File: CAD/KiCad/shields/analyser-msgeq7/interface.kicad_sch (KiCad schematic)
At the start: 3 parts

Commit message: Route the shield set and validate shared interfaces
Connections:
- net +5V: no longer names the net of JA1.23
- no-connect marks 0 -> 1
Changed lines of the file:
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@@
 (kicad_sch (version 20250114) (generator "eeschema") (generator_version "9.0")
  (paper "A3")
-          (title_block (title "analyser-msgeq7 / interface") (date "2026-10-01") (rev "A-review")
+          (title_block (title "analyser-msgeq7 / interface") (date "2026-10-04") (rev "A-prototype")
             (company "Colloquy of Mobiles") (comment 1 "Prototype: verify harness polarity and sensor values before connection"))
           (text "COLLOQUY / ANALYSER-MSGEQ7 / INTERFACE" (at 15.24 15.24 0) (effects (font (size 2.032 2.032) (bold yes)) (justify left top)))
@@
 (wire (pts (xy 121.9200 104.1400) (xy 124.4600 104.1400)) (stroke (width 0) (type default)))
 (global_label "GND" (shape bidirectional) (at 124.4600 104.1400 0) (effects (font (size 0.95 0.95)) (justify left)) (property "Intersheetrefs" "${INTERSHEET_REFS}" (at 124.4600 104.1400 0) (effects (font (size 1.016 1.016))  (hide yes))))
-(wire (pts (xy 121.9200 109.2200) (xy 124.4600 109.2200)) (stroke (width 0) (type default)))
-(global_label "+5V" (shape bidirectional) (at 124.4600 109.2200 0) (effects (font (size 0.95 0.95)) (justify left)) (property "Intersheetrefs" "${INTERSHEET_REFS}" (at 124.4600 109.2200 0) (effects (font (size 1.016 1.016))  (hide yes))))
+(no_connect (at 121.9200 109.2200))
 (symbol (lib_id "Colloquy:H1") (at 66.0400 154.9400 0) (unit 1) (exclude_from_sim no) (in_bom no) (on_board yes) (dnp no)
 (property "Reference" "H1" (at 66.0400 139.7000 0) (effects (font (size 1.016 1.016))  ))

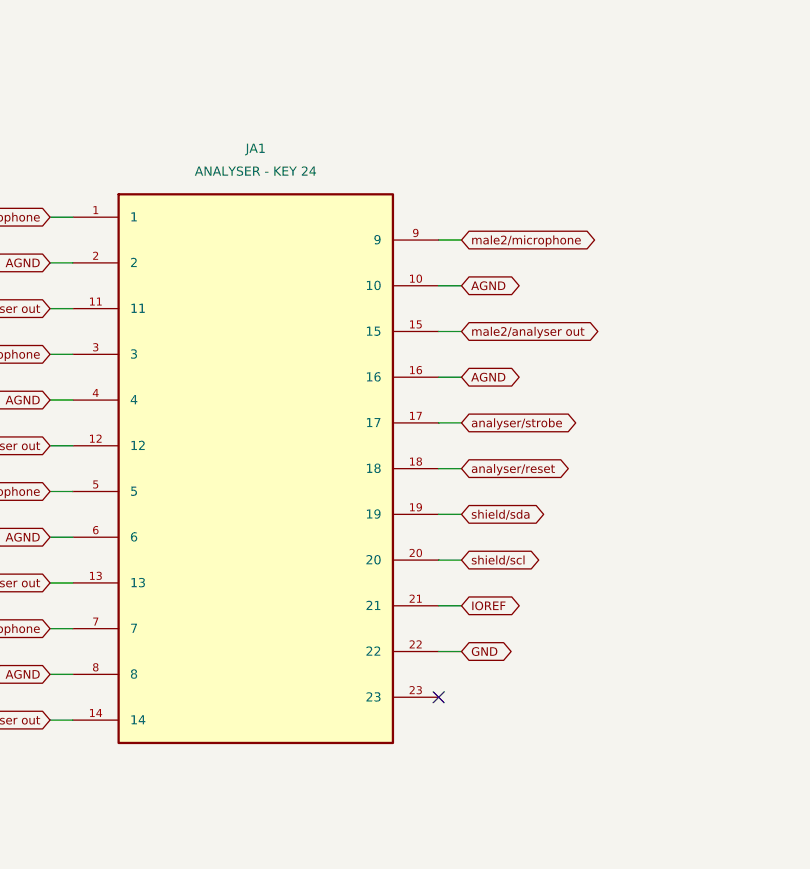
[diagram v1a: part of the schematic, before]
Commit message: Remove shield identification and adopt the simplified connector and Teensy pin maps
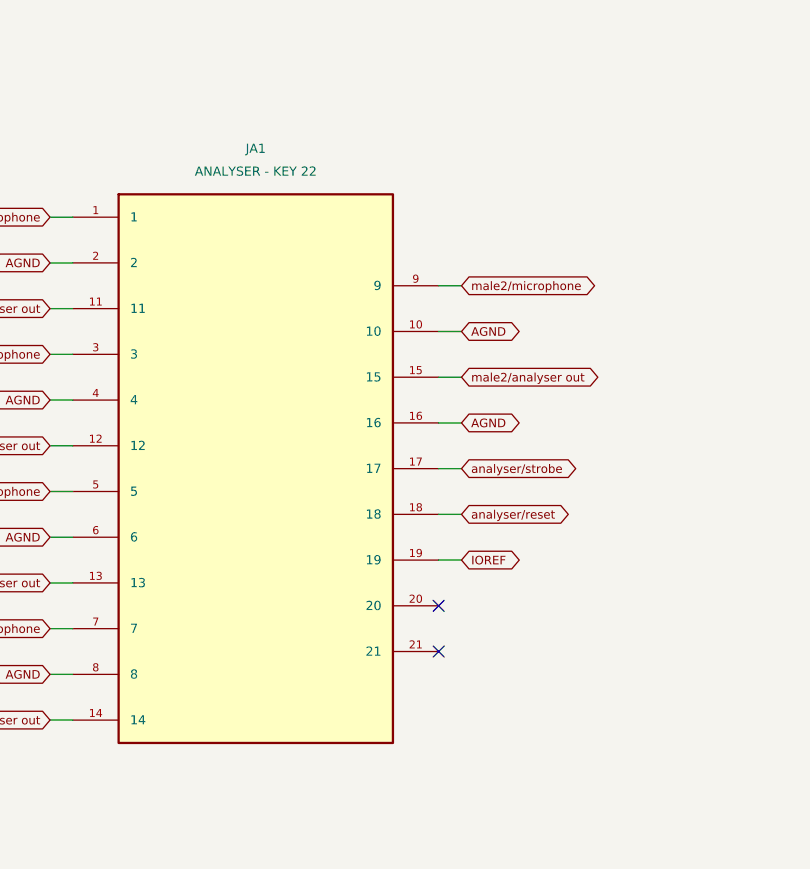
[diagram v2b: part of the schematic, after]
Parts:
- JA1: value ANALYSER - KEY 24 -> ANALYSER - KEY 22; footprint Shields:Socket_2x12_Key24 -> Shields:Socket_2x11_Key22
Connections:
- net shield/sda is gone; now on net IOREF: JA1.19
- net IOREF: no longer JA1.21
- removed net GND: JA1.22
- net shield/scl: no longer names the net of JA1.20
- no-connect marks 1 -> 2
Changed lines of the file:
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@@
 (symbol (lib_id "Colloquy:JA1") (at 101.6000 83.8200 0) (unit 1) (exclude_from_sim no) (in_bom yes) (on_board yes) (dnp no)
 (property "Reference" "JA1" (at 101.6000 48.2600 0) (effects (font (size 1.016 1.016))  ))
-(property "Value" "ANALYSER - KEY 24" (at 101.6000 50.8000 0) (effects (font (size 1.016 1.016))  ))
-(property "Footprint" "Shields:Socket_2x12_Key24" (at 101.6000 83.8200 0) (effects (font (size 1.27 1.27))  (hide yes)))
+(property "Value" "ANALYSER - KEY 22" (at 101.6000 50.8000 0) (effects (font (size 1.016 1.016))  ))
+(property "Footprint" "Shields:Socket_2x11_Key22" (at 101.6000 83.8200 0) (effects (font (size 1.27 1.27))  (hide yes)))
 (property "Datasheet" "" (at 101.6000 83.8200 0) (effects (font (size 1.27 1.27))  (hide yes)))
 (property "Description" "" (at 101.6000 83.8200 0) (effects (font (size 1.27 1.27))  (hide yes)))
@@
 (pin "20")
 (pin "21")
-(pin "22")
-(pin "23")
 (instances (project "analyser-msgeq7" (path "/051aa90c-bb55-5623-9e53-94470bed9b3c/ced2d10e-bbf6-59f9-8dd2-3b8fbcd538e9" (reference "JA1") (unit 1)))))
 (wire (pts (xy 81.2800 55.8800) (xy 78.7400 55.8800)) (stroke (width 0) (type default)))
@@
 (wire (pts (xy 81.2800 111.7600) (xy 78.7400 111.7600)) (stroke (width 0) (type default)))
 (global_label "male1/analyser out" (shape bidirectional) (at 78.7400 111.7600 180) (effects (font (size 0.95 0.95)) (justify right)) (property "Intersheetrefs" "${INTERSHEET_REFS}" (at 78.7400 111.7600 0) (effects (font (size 1.016 1.016))  (hide yes))))
-(wire (pts (xy 121.9200 58.4200) (xy 124.4600 58.4200)) (stroke (width 0) (type default)))
-(global_label "male2/microphone" (shape bidirectional) (at 124.4600 58.4200 0) (effects (font (size 0.95 0.95)) (justify left)) (property "Intersheetrefs" "${INTERSHEET_REFS}" (at 124.4600 58.4200 0) (effects (font (size 1.016 1.016))  (hide yes))))
 (wire (pts (xy 121.9200 63.5000) (xy 124.4600 63.5000)) (stroke (width 0) (type default)))
-(global_label "AGND" (shape bidirectional) (at 124.4600 63.5000 0) (effects (font (size 0.95 0.95)) (justify left)) (property "Intersheetrefs" "${INTERSHEET_REFS}" (at 124.4600 63.5000 0) (effects (font (size 1.016 1.016))  (hide yes))))
+(global_label "male2/microphone" (shape bidirectional) (at 124.4600 63.5000 0) (effects (font (size 0.95 0.95)) (justify left)) (property "Intersheetrefs" "${INTERSHEET_REFS}" (at 124.4600 63.5000 0) (effects (font (size 1.016 1.016))  (hide yes))))
 (wire (pts (xy 121.9200 68.5800) (xy 124.4600 68.5800)) (stroke (width 0) (type default)))
-(global_label "male2/analyser out" (shape bidirectional) (at 124.4600 68.5800 0) (effects (font (size 0.95 0.95)) (justify left)) (property "Intersheetrefs" "${INTERSHEET_REFS}" (at 124.4600 68.5800 0) (effects (font (size 1.016 1.016))  (hide yes))))
+(global_label "AGND" (shape bidirectional) (at 124.4600 68.5800 0) (effects (font (size 0.95 0.95)) (justify left)) (property "Intersheetrefs" "${INTERSHEET_REFS}" (at 124.4600 68.5800 0) (effects (font (size 1.016 1.016))  (hide yes))))
 (wire (pts (xy 121.9200 73.6600) (xy 124.4600 73.6600)) (stroke (width 0) (type default)))
-(global_label "AGND" (shape bidirectional) (at 124.4600 73.6600 0) (effects (font (size 0.95 0.95)) (justify left)) (property "Intersheetrefs" "${INTERSHEET_REFS}" (at 124.4600 73.6600 0) (effects (font (size 1.016 1.016))  (hide yes))))
+(global_label "male2/analyser out" (shape bidirectional) (at 124.4600 73.6600 0) (effects (font (size 0.95 0.95)) (justify left)) (property "Intersheetrefs" "${INTERSHEET_REFS}" (at 124.4600 73.6600 0) (effects (font (size 1.016 1.016))  (hide yes))))
 (wire (pts (xy 121.9200 78.7400) (xy 124.4600 78.7400)) (stroke (width 0) (type default)))
-(global_label "analyser/strobe" (shape bidirectional) (at 124.4600 78.7400 0) (effects (font (size 0.95 0.95)) (justify left)) (property "Intersheetrefs" "${INTERSHEET_REFS}" (at 124.4600 78.7400 0) (effects (font (size 1.016 1.016))  (hide yes))))
+(global_label "AGND" (shape bidirectional) (at 124.4600 78.7400 0) (effects (font (size 0.95 0.95)) (justify left)) (property "Intersheetrefs" "${INTERSHEET_REFS}" (at 124.4600 78.7400 0) (effects (font (size 1.016 1.016))  (hide yes))))
 (wire (pts (xy 121.9200 83.8200) (xy 124.4600 83.8200)) (stroke (width 0) (type default)))
-(global_label "analyser/reset" (shape bidirectional) (at 124.4600 83.8200 0) (effects (font (size 0.95 0.95)) (justify left)) (property "Intersheetrefs" "${INTERSHEET_REFS}" (at 124.4600 83.8200 0) (effects (font (size 1.016 1.016))  (hide yes))))
+(global_label "analyser/strobe" (shape bidirectional) (at 124.4600 83.8200 0) (effects (font (size 0.95 0.95)) (justify left)) (property "Intersheetrefs" "${INTERSHEET_REFS}" (at 124.4600 83.8200 0) (effects (font (size 1.016 1.016))  (hide yes))))
 (wire (pts (xy 121.9200 88.9000) (xy 124.4600 88.9000)) (stroke (width 0) (type default)))
-(global_label "shield/sda" (shape bidirectional) (at 124.4600 88.9000 0) (effects (font (size 0.95 0.95)) (justify left)) (property "Intersheetrefs" "${INTERSHEET_REFS}" (at 124.4600 88.9000 0) (effects (font (size 1.016 1.016))  (hide yes))))
+(global_label "analyser/reset" (shape bidirectional) (at 124.4600 88.9000 0) (effects (font (size 0.95 0.95)) (justify left)) (property "Intersheetrefs" "${INTERSHEET_REFS}" (at 124.4600 88.9000 0) (effects (font (size 1.016 1.016))  (hide yes))))
 (wire (pts (xy 121.9200 93.9800) (xy 124.4600 93.9800)) (stroke (width 0) (type default)))
-(global_label "shield/scl" (shape bidirectional) (at 124.4600 93.9800 0) (effects (font (size 0.95 0.95)) (justify left)) (property "Intersheetrefs" "${INTERSHEET_REFS}" (at 124.4600 93.9800 0) (effects (font (size 1.016 1.016))  (hide yes))))
-(wire (pts (xy 121.9200 99.0600) (xy 124.4600 99.0600)) (stroke (width 0) (type default)))
-(global_label "IOREF" (shape bidirectional) (at 124.4600 99.0600 0) (effects (font (size 0.95 0.95)) (justify left)) (property "Intersheetrefs" "${INTERSHEET_REFS}" (at 124.4600 99.0600 0) (effects (font (size 1.016 1.016))  (hide yes))))
-(wire (pts (xy 121.9200 104.1400) (xy 124.4600 104.1400)) (stroke (width 0) (type default)))
-(global_label "GND" (shape bidirectional) (at 124.4600 104.1400 0) (effects (font (size 0.95 0.95)) (justify left)) (property "Intersheetrefs" "${INTERSHEET_REFS}" (at 124.4600 104.1400 0) (effects (font (size 1.016 1.016))  (hide yes))))
-(no_connect (at 121.9200 109.2200))
+(global_label "IOREF" (shape bidirectional) (at 124.4600 93.9800 0) (effects (font (size 0.95 0.95)) (justify left)) (property "Intersheetrefs" "${INTERSHEET_REFS}" (at 124.4600 93.9800 0) (effects (font (size 1.016 1.016))  (hide yes))))
+(no_connect (at 121.9200 99.0600))
+(no_connect (at 121.9200 104.1400))
 (symbol (lib_id "Colloquy:H1") (at 66.0400 154.9400 0) (unit 1) (exclude_from_sim no) (in_bom no) (on_board yes) (dnp no)
 (property "Reference" "H1" (at 66.0400 139.7000 0) (effects (font (size 1.016 1.016))  ))

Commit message: Route microphones directly to Teensy and remove the analyser buffer board
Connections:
- net IOREF renamed MEGA_5V
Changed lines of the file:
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@@
 (kicad_sch (version 20250114) (generator "eeschema") (generator_version "9.0")
  (paper "A3")
-          (title_block (title "analyser-msgeq7 / interface") (date "2026-10-04") (rev "A-prototype")
+          (title_block (title "analyser-msgeq7 / interface") (date "2026-10-05") (rev "A-prototype")
             (company "Colloquy of Mobiles") (comment 1 "Prototype: verify harness polarity and sensor values before connection"))
           (text "COLLOQUY / ANALYSER-MSGEQ7 / INTERFACE" (at 15.24 15.24 0) (effects (font (size 2.032 2.032) (bold yes)) (justify left top)))
@@
 (global_label "analyser/reset" (shape bidirectional) (at 124.4600 88.9000 0) (effects (font (size 0.95 0.95)) (justify left)) (property "Intersheetrefs" "${INTERSHEET_REFS}" (at 124.4600 88.9000 0) (effects (font (size 1.016 1.016))  (hide yes))))
 (wire (pts (xy 121.9200 93.9800) (xy 124.4600 93.9800)) (stroke (width 0) (type default)))
-(global_label "IOREF" (shape bidirectional) (at 124.4600 93.9800 0) (effects (font (size 0.95 0.95)) (justify left)) (property "Intersheetrefs" "${INTERSHEET_REFS}" (at 124.4600 93.9800 0) (effects (font (size 1.016 1.016))  (hide yes))))
+(global_label "MEGA_5V" (shape bidirectional) (at 124.4600 93.9800 0) (effects (font (size 0.95 0.95)) (justify left)) (property "Intersheetrefs" "${INTERSHEET_REFS}" (at 124.4600 93.9800 0) (effects (font (size 1.016 1.016))  (hide yes))))
 (no_connect (at 121.9200 99.0600))
 (no_connect (at 121.9200 104.1400))
